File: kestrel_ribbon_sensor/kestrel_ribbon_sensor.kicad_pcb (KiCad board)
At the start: 4 copper layers, 48 x 48 mm, 26 parts, among them J1 SHF-120-01-L-D-SM, J2 SHF-120-01-L-D-SM, J3 DEBUG_HEADER

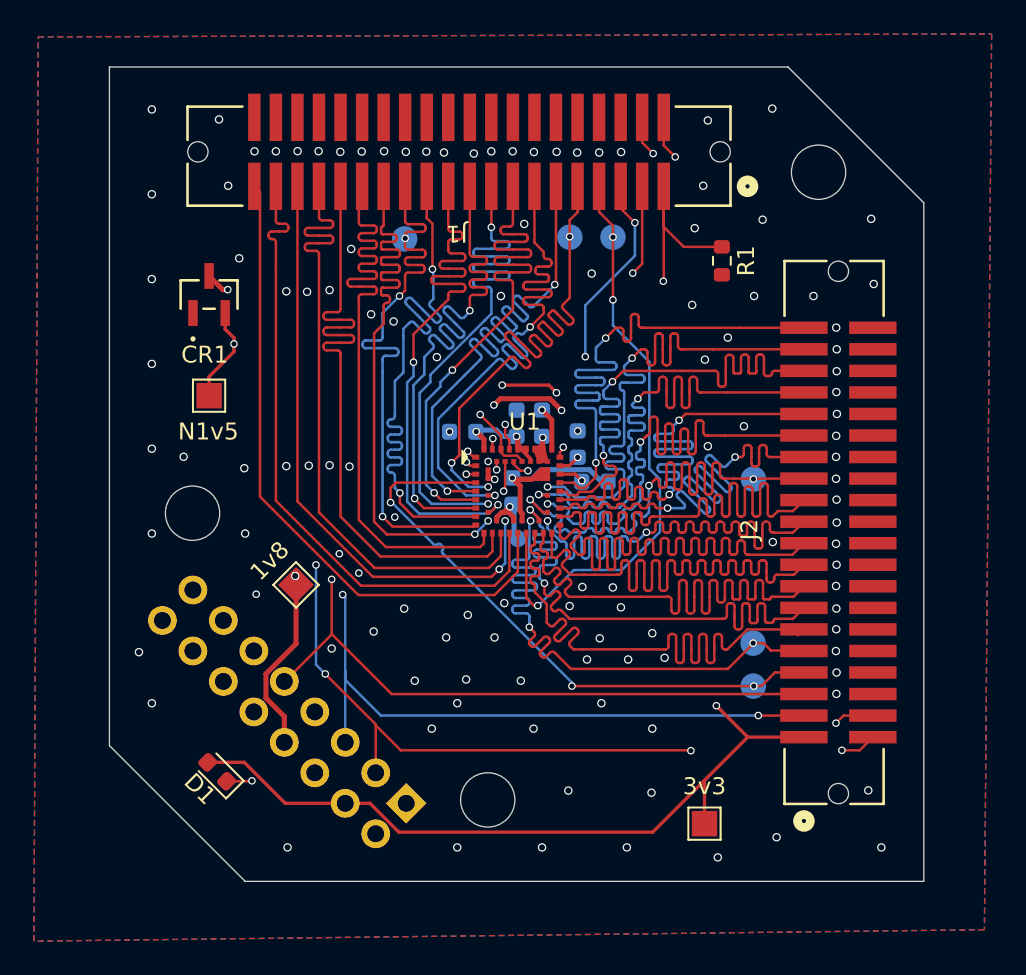
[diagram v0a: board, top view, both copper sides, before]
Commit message: fmc adapter redesign, add silkscreen to both pcbs
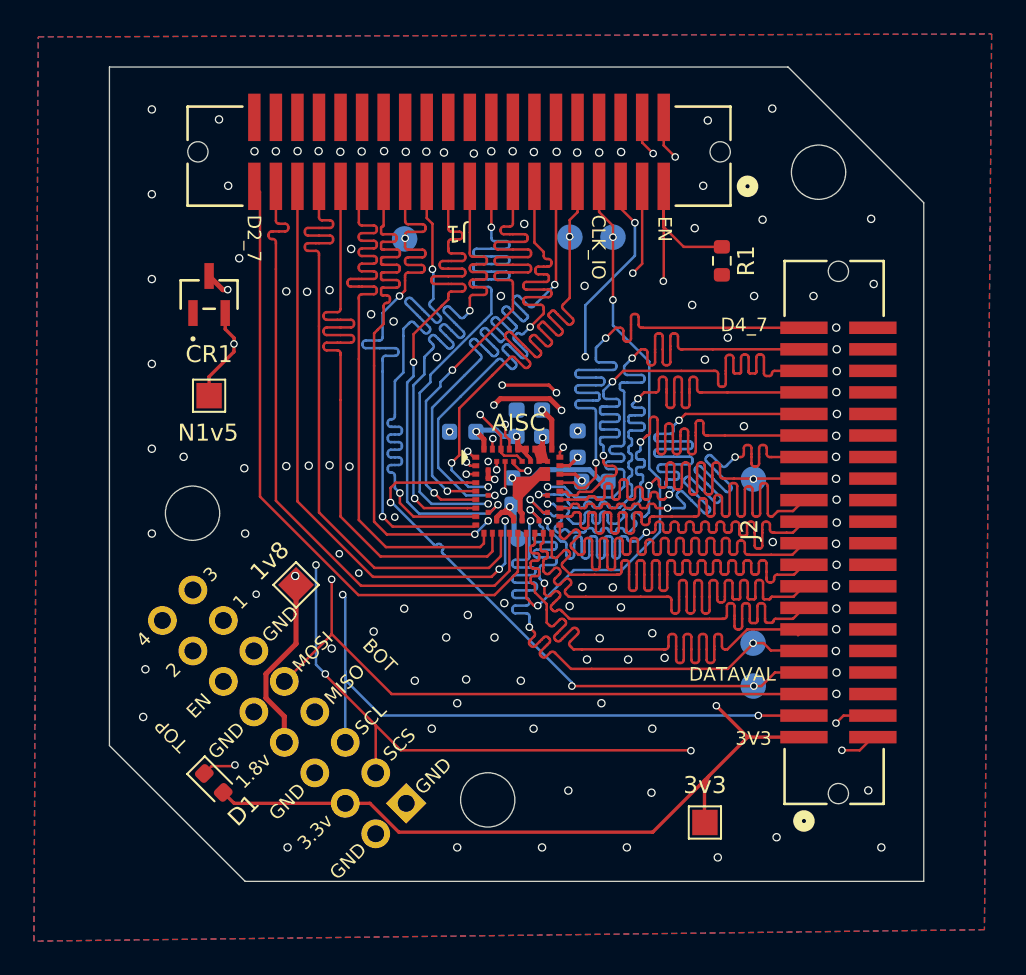
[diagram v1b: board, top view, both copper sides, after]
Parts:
- added G***: LOGO, LOGO, B.Cu at (151.0, 74.3)
- moved D1 0.68 mm to (145.7, 99.7), turned to -45 degrees
- moved 3v3 0.07 mm to (174.6, 102.0)
- renumbered U1 to AISC, CLK to CLK_IO, VAL to DATAVAL
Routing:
- net GND: track 21.7 -> 26.4 mm
- net /V3V3: track 68.3 -> 66.6 mm
- net Net-(D1-K): track 30.1 -> 31.2 mm
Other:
- board text added: "1"
- board text added: "1.8v"
- board text added: "2"
- board text added: "3"
- board text added: "3.3v"
- board text added: "3V3"
- board text added: "4"
- board text added: "AISC110C INTERFACE V1.1 NEWMAN & RAMOS WWU EECE 2026"
- board text added: "BOT"
- board text added: "CLK_IO"
- board text added: "D2_7"
- board text added: "D4_7"
- board text added: "DATAVAL"
- board text added: "EN"
- board text added: "GND"
- board text added: "KESTREL"
- board text added: "MISO"
- board text added: "MOSI"
- board text added: "SCL"
- board text added: "SCS"
- board text added: "TOP"
